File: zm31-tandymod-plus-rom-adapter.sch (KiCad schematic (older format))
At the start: 3 parts, among them SW1 SW_DPDT_x2, U1 74LS157, U2 27C512

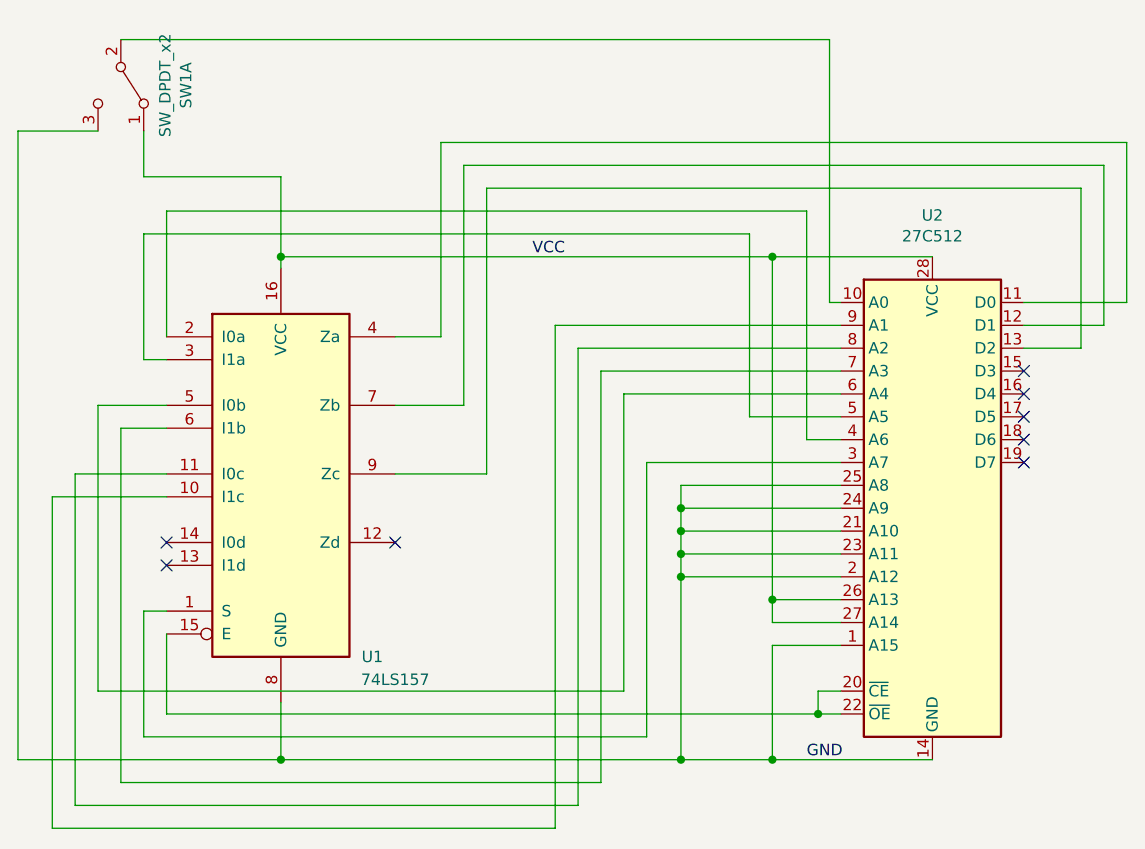
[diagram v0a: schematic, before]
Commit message: Label the nets
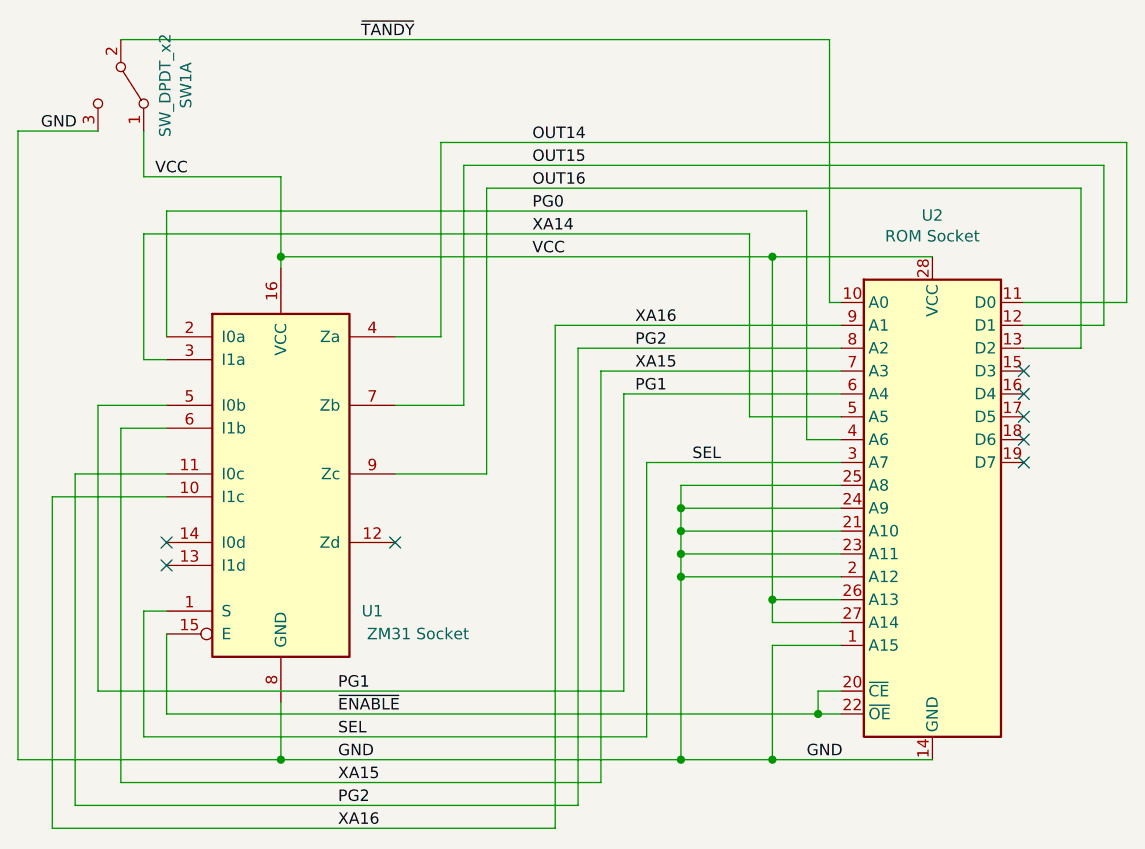
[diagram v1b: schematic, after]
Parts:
- U1: value 74LS157 -> ZM31 Socket
- U2: value 27C512 -> ROM Socket
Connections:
- net SEL: now reaches U1.1 (S), U2.3 (A7)
- net XA16: now reaches U1.10 (I1c), U2.9 (A1)
- net PG2: now reaches U1.11 (I0c), U2.8 (A2)
- net ~ENABLE: now reaches U1.15 (E), U2.20 (~CE), U2.22 (~OE)
- net PG0: now reaches U1.2 (I0a), U2.4 (A6)
- net XA14: now reaches U1.3 (I1a), U2.5 (A5)
- net OUT14: now reaches U1.4 (Za), U2.11 (D0)
- net PG1: now reaches U1.5 (I0b), U2.6 (A4)
- net XA15: now reaches U1.6 (I1b), U2.7 (A3)
- net OUT15: now reaches U1.7 (Zb), U2.12 (D1)
- net OUT16: now reaches U1.9 (Zc), U2.13 (D2)
- net ~TANDY: now reaches SW1.2 (B), U2.10 (A0)
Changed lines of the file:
@@
 EESchema Schematic File Version 4
+LIBS:zm31-tandymod-plus-rom-adapter-cache
 EELAYER 29 0
 EELAYER END
@@
 U 1 1 5DA3C72D
 P 2850 3200
-F 0 "U1" H 3250 2400 50  0000 C CNN
-F 1 "74LS157" H 3350 2300 50  0000 C CNN
+F 0 "U1" H 3250 2600 50  0000 C CNN
+F 1 "ZM31 Socket" H 3450 2500 50  0000 C CNN
 F 2 "Package_DIP:DIP-16_W7.62mm_Socket_LongPads" H 2850 3200 50  0001 C CNN
 F 3 "http://www.ti.com/lit/gpn/sn74LS157" H 2850 3200 50  0001 C CNN
@@
 P 5700 3350
 F 0 "U2" H 5700 4631 50  0000 C CNN
-F 1 "27C512" H 5700 4540 50  0000 C CNN
+F 1 "ROM Socket" H 5700 4540 50  0000 C CNN
 F 2 "Package_DIP:DIP-28_W15.24mm_Socket_LongPads" H 5700 3350 50  0001 C CNN
 F 3 "http://ww1.microchip.com/downloads/en/DeviceDoc/doc0015.pdf" H 5700 3350 50  0001 C CNN
@@
 Text Label 5150 4450 0    50   ~ 0
 GND
+Text Label 3200 1300 0    50   ~ 0
+~TANDY
+Text Label 3100 4750 0    50   ~ 0
+XA16
+Text Label 3100 4650 0    50   ~ 0
+PG2
+Text Label 3100 4550 0    50   ~ 0
+XA15
+Text Label 3100 4450 0    50   ~ 0
+GND
+Text Label 3100 4350 0    50   ~ 0
+SEL
+Text Label 3100 4250 0    50   ~ 0
+~ENABLE
+Text Label 3100 4150 0    50   ~ 0
+PG1
+Text Label 4400 2850 0    50   ~ 0
+PG1
+Text Label 4400 2750 0    50   ~ 0
+XA15
+Text Label 4400 2650 0    50   ~ 0
+PG2
+Text Label 4400 2550 0    50   ~ 0
+XA16
+Text Label 3950 2150 0    50   ~ 0
+XA14
+Text Label 3950 2050 0    50   ~ 0
+PG0
+Text Label 3950 1750 0    50   ~ 0
+OUT14
+Text Label 3950 1850 0    50   ~ 0
+OUT15
+Text Label 3950 1950 0    50   ~ 0
+OUT16
+Text Label 2300 1900 0    50   ~ 0
+VCC
+Text Label 1800 1700 0    50   ~ 0
+GND
+Text Label 4650 3150 0    50   ~ 0
+SEL
 $EndSCHEMATC
